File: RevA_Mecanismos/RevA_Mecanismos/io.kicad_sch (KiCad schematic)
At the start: 3 parts, among them J10 Conn_01x02_Pin, J8 Conn_01x08_Pin, J9 Conn_01x02_Pin

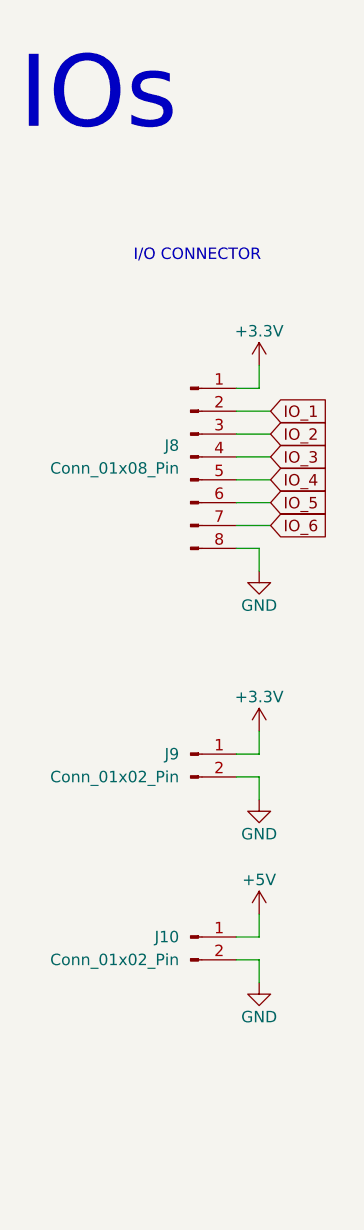
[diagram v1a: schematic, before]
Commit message: Updated STM32 USV Mechanism PCB
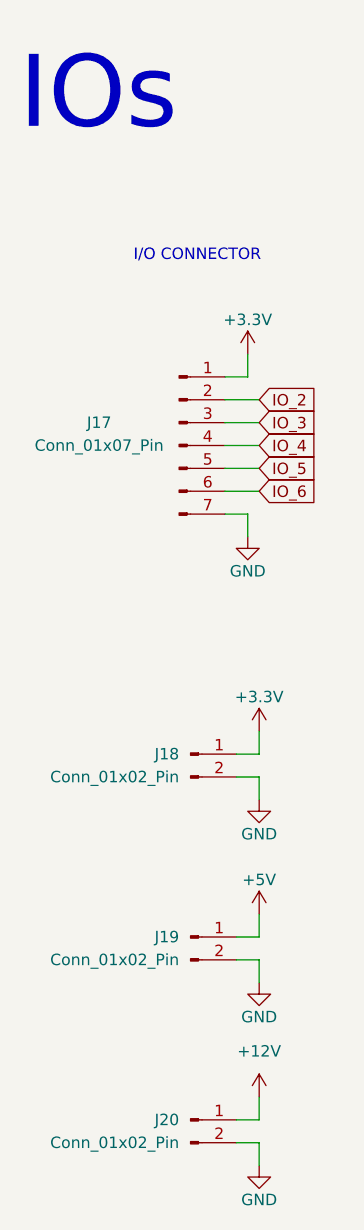
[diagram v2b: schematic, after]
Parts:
- removed J8: Conn_01x08_Pin, Connector_PinHeader_2.54mm:PinHeader_1x08_P2.54mm_Vertical, symbol Connector:Conn_01x08_Pin
- added J17: Conn_01x07_Pin, Connector_PinHeader_2.54mm:PinHeader_1x07_P2.54mm_Vertical, symbol Connector:Conn_01x07_Pin
- added J20: Conn_01x02_Pin, Connector_PinHeader_2.54mm:PinHeader_1x02_P2.54mm_Vertical, symbol Connector:Conn_01x02_Pin
- renumbered J9 to J18, J10 to J19
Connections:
- net +3.3V: now also J17.1 (Pin_1)
- net GND: now also J17.7 (Pin_7), J20.2 (Pin_2)
- net IO_2: now also J17.2 (Pin_2)
- net IO_3: now also J17.3 (Pin_3)
- net IO_4: now also J17.4 (Pin_4)
- net IO_5: now also J17.5 (Pin_5)
- net IO_6: now also J17.6 (Pin_6)
- new net +12V: J20.1 (Pin_1)

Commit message: Complete schematic and pcb designs, routes missing and not yet complete
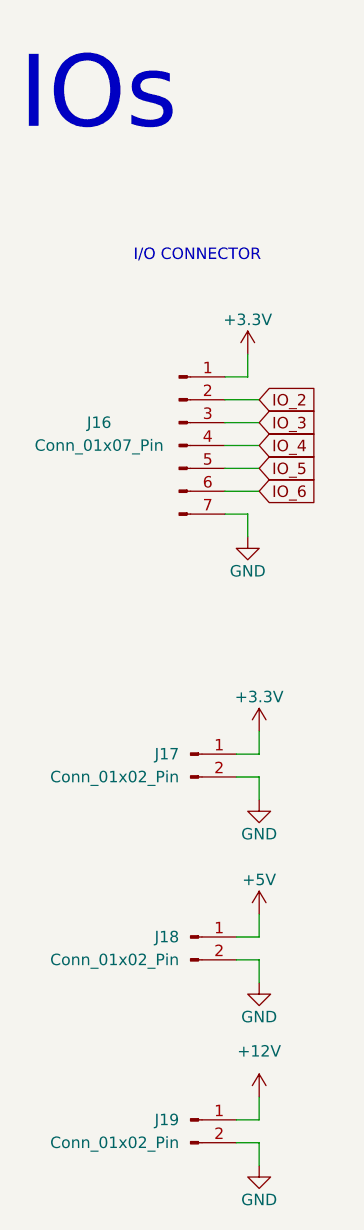
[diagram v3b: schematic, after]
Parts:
- J16: renamed from J17; footprint Connector_PinHeader_2.54mm:PinHeader_1x07_P2.54mm_Vertical -> Connector_PinHeader_2.54mm:PinHeader_1x02_P2.54mm_Vertical
- J17: renamed from J18; footprint Connector_PinHeader_2.54mm:PinHeader_1x02_P2.54mm_Vertical -> 36-3557-2-ND:CONN_3557-2_KEY
- J18: renamed from J19; footprint Connector_PinHeader_2.54mm:PinHeader_1x02_P2.54mm_Vertical -> Connector_PinHeader_2.54mm:PinHeader_1x04_P2.54mm_Vertical
- J19: renamed from J20; footprint Connector_PinHeader_2.54mm:PinHeader_1x02_P2.54mm_Vertical -> Connector_PinHeader_2.54mm:PinHeader_1x04_P2.54mm_Vertical
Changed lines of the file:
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@@
   (symbol (lib_id "power:GND") (at 49.53 147.32 0) (unit 1)
     (in_bom yes) (on_board yes) (dnp no)
-    (property "Reference" "#PWR0100" (at 49.53 153.67 0)
+    (property "Reference" "#PWR097" (at 49.53 153.67 0)
       (effects (font (size 1.27 1.27)) hide)
     )
@@
       (project "RevA_Mecanismos"
         (path "/3a16a434-10b7-49a8-988b-273362cb395e/55ce433e-e66f-484d-abbf-48bede5ad817"
-          (reference "#PWR0100") (unit 1)
+          (reference "#PWR097") (unit 1)
         )
       )
@@
   (symbol (lib_id "Connector:Conn_01x02_Pin") (at 41.91 121.92 0) (unit 1)
     (in_bom yes) (on_board yes) (dnp no)
-    (property "Reference" "J19" (at 40.64 121.92 0)
+    (property "Reference" "J18" (at 40.64 121.92 0)
       (effects (font (size 1.27 1.27)) (justify right))
     )
@@
       (effects (font (size 1.27 1.27)) (justify right))
     )
-    (property "Footprint" "Connector_PinHeader_2.54mm:PinHeader_1x02_P2.54mm_Vertical" (at 41.91 121.92 0)
+    (property "Footprint" "Connector_PinHeader_2.54mm:PinHeader_1x04_P2.54mm_Vertical" (at 41.91 121.92 0)
       (effects (font (size 1.27 1.27)) hide)
     )
@@
       (project "RevA_Mecanismos"
         (path "/3a16a434-10b7-49a8-988b-273362cb395e/55ce433e-e66f-484d-abbf-48bede5ad817"
-          (reference "J19") (unit 1)
+          (reference "J18") (unit 1)
         )
       )
@@
   (symbol (lib_id "power:GND") (at 49.53 127 0) (unit 1)
     (in_bom yes) (on_board yes) (dnp no)
-    (property "Reference" "#PWR098" (at 49.53 133.35 0)
+    (property "Reference" "#PWR095" (at 49.53 133.35 0)
       (effects (font (size 1.27 1.27)) hide)
     )
@@
       (project "RevA_Mecanismos"
         (path "/3a16a434-10b7-49a8-988b-273362cb395e/55ce433e-e66f-484d-abbf-48bede5ad817"
-          (reference "#PWR098") (unit 1)
+          (reference "#PWR095") (unit 1)
         )
       )
@@
   (symbol (lib_id "power:+3.3V") (at 49.53 99.06 0) (unit 1)
     (in_bom yes) (on_board yes) (dnp no) (fields_autoplaced)
-    (property "Reference" "#PWR095" (at 49.53 102.87 0)
+    (property "Reference" "#PWR092" (at 49.53 102.87 0)
       (effects (font (size 1.27 1.27)) hide)
     )
@@
       (project "RevA_Mecanismos"
         (path "/3a16a434-10b7-49a8-988b-273362cb395e/55ce433e-e66f-484d-abbf-48bede5ad817"
-          (reference "#PWR095") (unit 1)
+          (reference "#PWR092") (unit 1)
         )
       )
@@
   (symbol (lib_id "Connector:Conn_01x02_Pin") (at 41.91 142.24 0) (unit 1)
     (in_bom yes) (on_board yes) (dnp no)
-    (property "Reference" "J20" (at 40.64 142.24 0)
+    (property "Reference" "J19" (at 40.64 142.24 0)
       (effects (font (size 1.27 1.27)) (justify right))
     )
@@
       (effects (font (size 1.27 1.27)) (justify right))
     )
-    (property "Footprint" "Connector_PinHeader_2.54mm:PinHeader_1x02_P2.54mm_Vertical" (at 41.91 142.24 0)
+    (property "Footprint" "Connector_PinHeader_2.54mm:PinHeader_1x04_P2.54mm_Vertical" (at 41.91 142.24 0)
       (effects (font (size 1.27 1.27)) hide)
     )
@@
       (project "RevA_Mecanismos"
         (path "/3a16a434-10b7-49a8-988b-273362cb395e/55ce433e-e66f-484d-abbf-48bede5ad817"
-          (reference "J20") (unit 1)
+          (reference "J19") (unit 1)
         )
       )
@@
   (symbol (lib_id "power:+5V") (at 49.53 119.38 0) (unit 1)
     (in_bom yes) (on_board yes) (dnp no) (fields_autoplaced)
-    (property "Reference" "#PWR097" (at 49.53 123.19 0)
+    (property "Reference" "#PWR094" (at 49.53 123.19 0)
       (effects (font (size 1.27 1.27)) hide)
     )
@@
       (project "RevA_Mecanismos"
         (path "/3a16a434-10b7-49a8-988b-273362cb395e/55ce433e-e66f-484d-abbf-48bede5ad817"
-          (reference "#PWR097") (unit 1)
+          (reference "#PWR094") (unit 1)
         )
       )
@@
   (symbol (lib_id "Connector:Conn_01x02_Pin") (at 41.91 101.6 0) (unit 1)
     (in_bom yes) (on_board yes) (dnp no)
-    (property "Reference" "J18" (at 40.64 101.6 0)
+    (property "Reference" "J17" (at 40.64 101.6 0)
       (effects (font (size 1.27 1.27)) (justify right))
     )
@@
       (effects (font (size 1.27 1.27)) (justify right))
     )
-    (property "Footprint" "Connector_PinHeader_2.54mm:PinHeader_1x02_P2.54mm_Vertical" (at 41.91 101.6 0)
+    (property "Footprint" "36-3557-2-ND:CONN_3557-2_KEY" (at 41.91 101.6 0)
       (effects (font (size 1.27 1.27)) hide)
     )
@@
       (project "RevA_Mecanismos"
         (path "/3a16a434-10b7-49a8-988b-273362cb395e/55ce433e-e66f-484d-abbf-48bede5ad817"
-          (reference "J18") (unit 1)
+          (reference "J17") (unit 1)
         )
       )
@@
   (symbol (lib_id "power:GND") (at 49.53 106.68 0) (unit 1)
     (in_bom yes) (on_board yes) (dnp no)
-    (property "Reference" "#PWR096" (at 49.53 113.03 0)
+    (property "Reference" "#PWR093" (at 49.53 113.03 0)
       (effects (font (size 1.27 1.27)) hide)
     )
@@
       (project "RevA_Mecanismos"
         (path "/3a16a434-10b7-49a8-988b-273362cb395e/55ce433e-e66f-484d-abbf-48bede5ad817"
+          (reference "#PWR093") (unit 1)
+        )
+      )
+    )
+  )
+  (symbol (lib_id "power:GND") (at 48.26 77.47 0) (unit 1)
+    (in_bom yes) (on_board yes) (dnp no)
+    (property "Reference" "#PWR091" (at 48.26 83.82 0)
+      (effects (font (size 1.27 1.27)) hide)
+    )
+    (property "Value" "GND" (at 48.26 81.28 0)
+      (effects (font (size 1.27 1.27)))
+    )
+    (property "Footprint" "" (at 48.26 77.47 0)
+      (effects (font (size 1.27 1.27)) hide)
+    )
+    (property "Datasheet" "" (at 48.26 77.47 0)
+      (effects (font (size 1.27 1.27)) hide)
+    )
+    (pin "1")
+    (instances
+      (project "RevA_Mecanismos"
+        (path "/3a16a434-10b7-49a8-988b-273362cb395e/55ce433e-e66f-484d-abbf-48bede5ad817"
+          (reference "#PWR091") (unit 1)
+        )
+      )
+    )
+  )
+  (symbol (lib_id "power:+12V") (at 49.53 139.7 0) (unit 1)
+    (in_bom yes) (on_board yes) (dnp no) (fields_autoplaced)
+    (property "Reference" "#PWR096" (at 49.53 143.51 0)
+      (effects (font (size 1.27 1.27)) hide)
+    )
+    (property "Value" "+12V" (at 49.53 134.62 0)
+      (effects (font (size 1.27 1.27)))
+    )
+    (property "Footprint" "" (at 49.53 139.7 0)
+      (effects (font (size 1.27 1.27)) hide)
+    )
+    (property "Datasheet" "" (at 49.53 139.7 0)
+      (effects (font (size 1.27 1.27)) hide)
+    )
+    (pin "1")
+    (instances
+      (project "RevA_Mecanismos"
+        (path "/3a16a434-10b7-49a8-988b-273362cb395e/55ce433e-e66f-484d-abbf-48bede5ad817"
           (reference "#PWR096") (unit 1)
         )
@@
     )
   )
-  (symbol (lib_id "power:GND") (at 48.26 77.47 0) (unit 1)
-    (in_bom yes) (on_board yes) (dnp no)
-    (property "Reference" "#PWR094" (at 48.26 83.82 0)
-      (effects (font (size 1.27 1.27)) hide)
-    )
-    (property "Value" "GND" (at 48.26 81.28 0)
-      (effects (font (size 1.27 1.27)))
-    )
-    (property "Footprint" "" (at 48.26 77.47 0)
-      (effects (font (size 1.27 1.27)) hide)
-    )
-    (property "Datasheet" "" (at 48.26 77.47 0)
-      (effects (font (size 1.27 1.27)) hide)
-    )
-    (pin "1")
-    (instances
-      (project "RevA_Mecanismos"
-        (path "/3a16a434-10b7-49a8-988b-273362cb395e/55ce433e-e66f-484d-abbf-48bede5ad817"
-          (reference "#PWR094") (unit 1)
-        )
-      )
-    )
-  )
-  (symbol (lib_id "power:+12V") (at 49.53 139.7 0) (unit 1)
-    (in_bom yes) (on_board yes) (dnp no) (fields_autoplaced)
-    (property "Reference" "#PWR099" (at 49.53 143.51 0)
-      (effects (font (size 1.27 1.27)) hide)
-    )
-    (property "Value" "+12V" (at 49.53 134.62 0)
-      (effects (font (size 1.27 1.27)))
-    )
-    (property "Footprint" "" (at 49.53 139.7 0)
-      (effects (font (size 1.27 1.27)) hide)
-    )
-    (property "Datasheet" "" (at 49.53 139.7 0)
-      (effects (font (size 1.27 1.27)) hide)
-    )
-    (pin "1")
-    (instances
-      (project "RevA_Mecanismos"
-        (path "/3a16a434-10b7-49a8-988b-273362cb395e/55ce433e-e66f-484d-abbf-48bede5ad817"
-          (reference "#PWR099") (unit 1)
-        )
-      )
-    )
-  )
   (symbol (lib_id "Connector:Conn_01x07_Pin") (at 40.64 67.31 0) (unit 1)
     (in_bom yes) (on_board yes) (dnp no)
-    (property "Reference" "J17" (at 31.75 64.77 0)
+    (property "Reference" "J16" (at 31.75 64.77 0)
       (effects (font (size 1.27 1.27)))
     )
@@
       (effects (font (size 1.27 1.27)))
     )
-    (property "Footprint" "Connector_PinHeader_2.54mm:PinHeader_1x07_P2.54mm_Vertical" (at 40.64 67.31 0)
+    (property "Footprint" "Connector_PinHeader_2.54mm:PinHeader_1x02_P2.54mm_Vertical" (at 40.64 67.31 0)
       (effects (font (size 1.27 1.27)) hide)
     )
@@
       (project "RevA_Mecanismos"
         (path "/3a16a434-10b7-49a8-988b-273362cb395e/55ce433e-e66f-484d-abbf-48bede5ad817"
-          (reference "J17") (unit 1)
+          (reference "J16") (unit 1)
         )
       )
@@
   (symbol (lib_id "power:+3.3V") (at 48.26 57.15 0) (unit 1)
     (in_bom yes) (on_board yes) (dnp no) (fields_autoplaced)
-    (property "Reference" "#PWR093" (at 48.26 60.96 0)
+    (property "Reference" "#PWR090" (at 48.26 60.96 0)
       (effects (font (size 1.27 1.27)) hide)
     )
@@
       (project "RevA_Mecanismos"
         (path "/3a16a434-10b7-49a8-988b-273362cb395e/55ce433e-e66f-484d-abbf-48bede5ad817"
-          (reference "#PWR093") (unit 1)
-        )
-      )
+          (reference "#PWR090") (unit 1)
+        )
+      )

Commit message: Corrections to component footprints in schematic design made during the development of BOM
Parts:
- J17: footprint 36-3557-2-ND:CONN_3557-2_KEY -> Connector_PinHeader_2.54mm:PinHeader_1x02_P2.54mm_Vertical
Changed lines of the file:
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@@
       (effects (font (size 1.27 1.27)) (justify right))
     )
-    (property "Footprint" "36-3557-2-ND:CONN_3557-2_KEY" (at 41.91 101.6 0)
+    (property "Footprint" "Connector_PinHeader_2.54mm:PinHeader_1x02_P2.54mm_Vertical" (at 41.91 101.6 0)
       (effects (font (size 1.27 1.27)) hide)
     )
